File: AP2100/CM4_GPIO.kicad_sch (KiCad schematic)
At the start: 27 parts, among them J1 Conn_01x03, J2 Conn_02x07_Odd_Even, J3 Conn_01x03, J8 THD-20-R, U5 74LVC1G07SE-7, U9 74LVC1G07SE-7

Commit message: Finish PoE section Rename CM4IO library as AP2100
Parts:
- Module1: footprint CM4IO:Raspberry-Pi-4-Compute-Module -> AP2100:Raspberry-Pi-4-Compute-Module; symbol CM4IO:ComputeModule4-CM4 -> AP2100:ComputeModule4-CM4
- U5, U9: symbol CM4IO:74LVC1G07_copy -> AP2100:74LVC1G07_copy
- U? (x4): symbol CM4IO:TPD4EUSB30 -> AP2100:TPD4EUSB30
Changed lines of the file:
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@@
   (junction (at 269.494 63.5) (diameter 1.016) (color 0 0 0 0))
   (junction (at 269.494 68.58) (diameter 1.016) (color 0 0 0 0))
+  (no_connect (at 147.955 109.22))
+  (no_connect (at 147.955 104.14))
+  (no_connect (at 39.37 144.78))
+  (no_connect (at 208.915 111.76))
+  (no_connect (at 208.915 43.18))
   (no_connect (at 147.955 99.06))
   (no_connect (at 147.955 106.68))
-  (no_connect (at 208.915 43.18))
-  (no_connect (at 208.915 111.76))
-  (no_connect (at 147.955 104.14))
-  (no_connect (at 39.37 144.78))
-  (no_connect (at 147.955 109.22))
   (wire (pts (xy 15.24 169.545) (xy 29.21 169.545))
     (stroke (width 0) (type solid) (color 0 0 0 0))
@@
   (symbol (lib_id "power:GND") (at 19.05 57.785 0) (unit 1)
     (in_bom yes) (on_board yes)
-    (property "Reference" "#PWR?" (id 0) (at 19.05 64.135 0)
+    (property "Reference" "#PWR0107" (id 0) (at 19.05 64.135 0)
       (effects (font (size 1.27 1.27)) hide)
     )
@@
   (symbol (lib_id "power:GND") (at 40.64 89.535 0) (unit 1)
     (in_bom yes) (on_board yes)
-    (property "Reference" "#PWR?" (id 0) (at 40.64 95.885 0)
+    (property "Reference" "#PWR0109" (id 0) (at 40.64 95.885 0)
       (effects (font (size 1.27 1.27)) hide)
     )
@@
   (symbol (lib_id "power:GND") (at 66.04 137.795 0) (unit 1)
     (in_bom yes) (on_board yes)
-    (property "Reference" "#PWR?" (id 0) (at 66.04 144.145 0)
+    (property "Reference" "#PWR0111" (id 0) (at 66.04 144.145 0)
       (effects (font (size 1.27 1.27)) hide)
     )
@@
   (symbol (lib_id "power:GND") (at 83.185 57.15 0) (mirror y) (unit 1)
     (in_bom yes) (on_board yes)
-    (property "Reference" "#PWR?" (id 0) (at 83.185 63.5 0)
+    (property "Reference" "#PWR0108" (id 0) (at 83.185 63.5 0)
       (effects (font (size 1.27 1.27)) hide)
     )
@@
   (symbol (lib_id "power:GND") (at 88.9 89.535 0) (unit 1)
     (in_bom yes) (on_board yes)
-    (property "Reference" "#PWR?" (id 0) (at 88.9 95.885 0)
+    (property "Reference" "#PWR0110" (id 0) (at 88.9 95.885 0)
       (effects (font (size 1.27 1.27)) hide)
     )
@@
   (symbol (lib_id "power:GND") (at 93.98 126.365 0) (unit 1)
     (in_bom yes) (on_board yes)
-    (property "Reference" "#PWR?" (id 0) (at 93.98 132.715 0)
+    (property "Reference" "#PWR0114" (id 0) (at 93.98 132.715 0)
       (effects (font (size 1.27 1.27)) hide)
     )
@@
   (symbol (lib_id "power:GND") (at 93.98 158.115 0) (unit 1)
     (in_bom yes) (on_board yes)
-    (property "Reference" "#PWR?" (id 0) (at 93.98 164.465 0)
+    (property "Reference" "#PWR0113" (id 0) (at 93.98 164.465 0)
       (effects (font (size 1.27 1.27)) hide)
     )
@@
     )
   )
-  (symbol (lib_id "CM4IO:74LVC1G07_copy") (at 29.21 177.165 0) (unit 1)
+  (symbol (lib_id "AP2100:74LVC1G07_copy") (at 29.21 177.165 0) (unit 1)
     (in_bom yes) (on_board yes)
     (property "Reference" "U9" (id 0) (at 31.75 170.815 0))
@@
     )
   )
-  (symbol (lib_id "CM4IO:74LVC1G07_copy") (at 152.4 180.34 0) (unit 1)
+  (symbol (lib_id "AP2100:74LVC1G07_copy") (at 152.4 180.34 0) (unit 1)
     (in_bom yes) (on_board yes)
     (property "Reference" "U5" (id 0) (at 153.924 177.8 0)
@@
     )
   )
-  (symbol (lib_id "CM4IO:TPD4EUSB30") (at 40.64 76.835 0) (unit 1)
+  (symbol (lib_id "AP2100:TPD4EUSB30") (at 40.64 76.835 0) (unit 1)
     (in_bom yes) (on_board yes)
     (property "Reference" "U?" (id 0) (at 40.64 64.9732 0))
@@
     )
   )
-  (symbol (lib_id "CM4IO:TPD4EUSB30") (at 88.9 76.835 0) (unit 1)
+  (symbol (lib_id "AP2100:TPD4EUSB30") (at 88.9 76.835 0) (unit 1)
     (in_bom yes) (on_board yes)
     (property "Reference" "U?" (id 0) (at 88.9 64.9732 0))
@@
     )
   )
-  (symbol (lib_id "CM4IO:TPD4EUSB30") (at 93.98 113.665 0) (unit 1)
+  (symbol (lib_id "AP2100:TPD4EUSB30") (at 93.98 113.665 0) (unit 1)
     (in_bom yes) (on_board yes)
     (property "Reference" "U?" (id 0) (at 93.98 101.8032 0))
@@
     )
   )
-  (symbol (lib_id "CM4IO:TPD4EUSB30") (at 93.98 145.415 0) (unit 1)
+  (symbol (lib_id "AP2100:TPD4EUSB30") (at 93.98 145.415 0) (unit 1)
     (in_bom yes) (on_board yes)
     (property "Reference" "U?" (id 0) (at 93.98 133.5532 0))
@@
     )
   )
-  (symbol (lib_id "CM4IO:ComputeModule4-CM4") (at 180.975 76.2 0) (unit 1)
+  (symbol (lib_id "AP2100:ComputeModule4-CM4") (at 180.975 76.2 0) (unit 1)
     (in_bom yes) (on_board yes)
     (property "Reference" "Module1" (id 0) (at 178.435 14.605 0))
     (property "Value" "ComputeModule4" (id 1) (at 178.435 16.9164 0))
-    (property "Footprint" "CM4IO:Raspberry-Pi-4-Compute-Module" (id 2) (at 323.215 102.87 0)
-      (effects (font (size 1.27 1.27)) hide)
-    )
+    (property "Footprint" "AP2100:Raspberry-Pi-4-Compute-Module" (id 2) (at 323.215 102.87 0)
+      (effects (font (size 1.27 1.27)) hide)
+    )

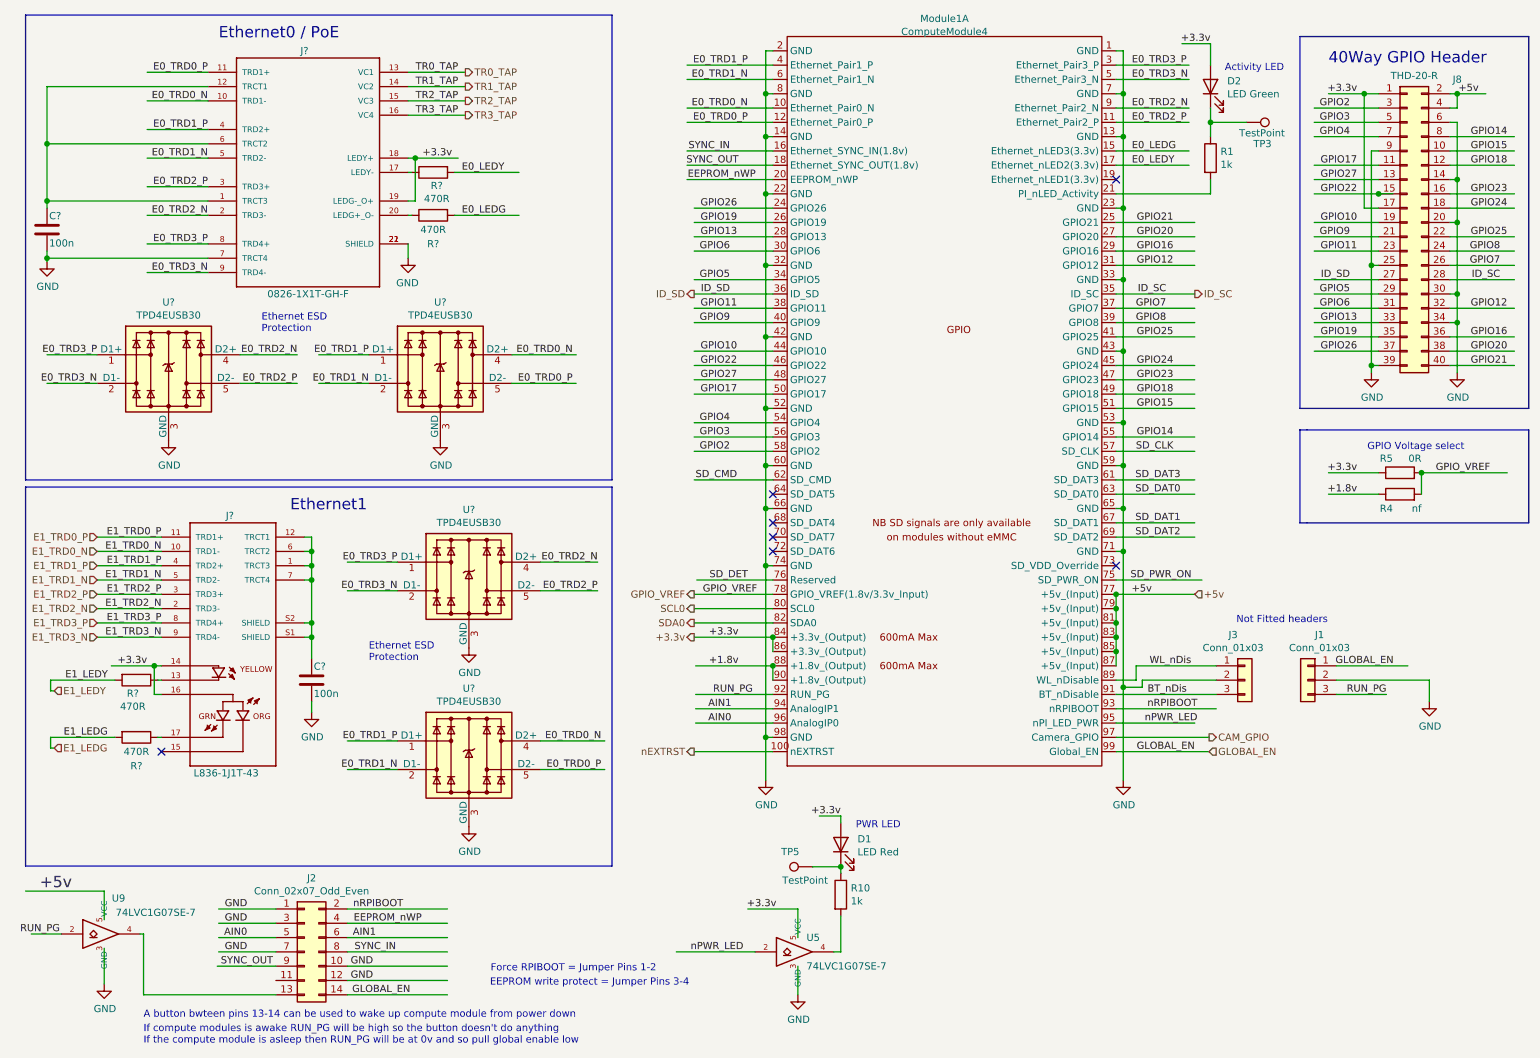
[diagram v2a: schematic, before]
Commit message: Add AP3000 single radio for security cameras. Add CM4IO Raspi board
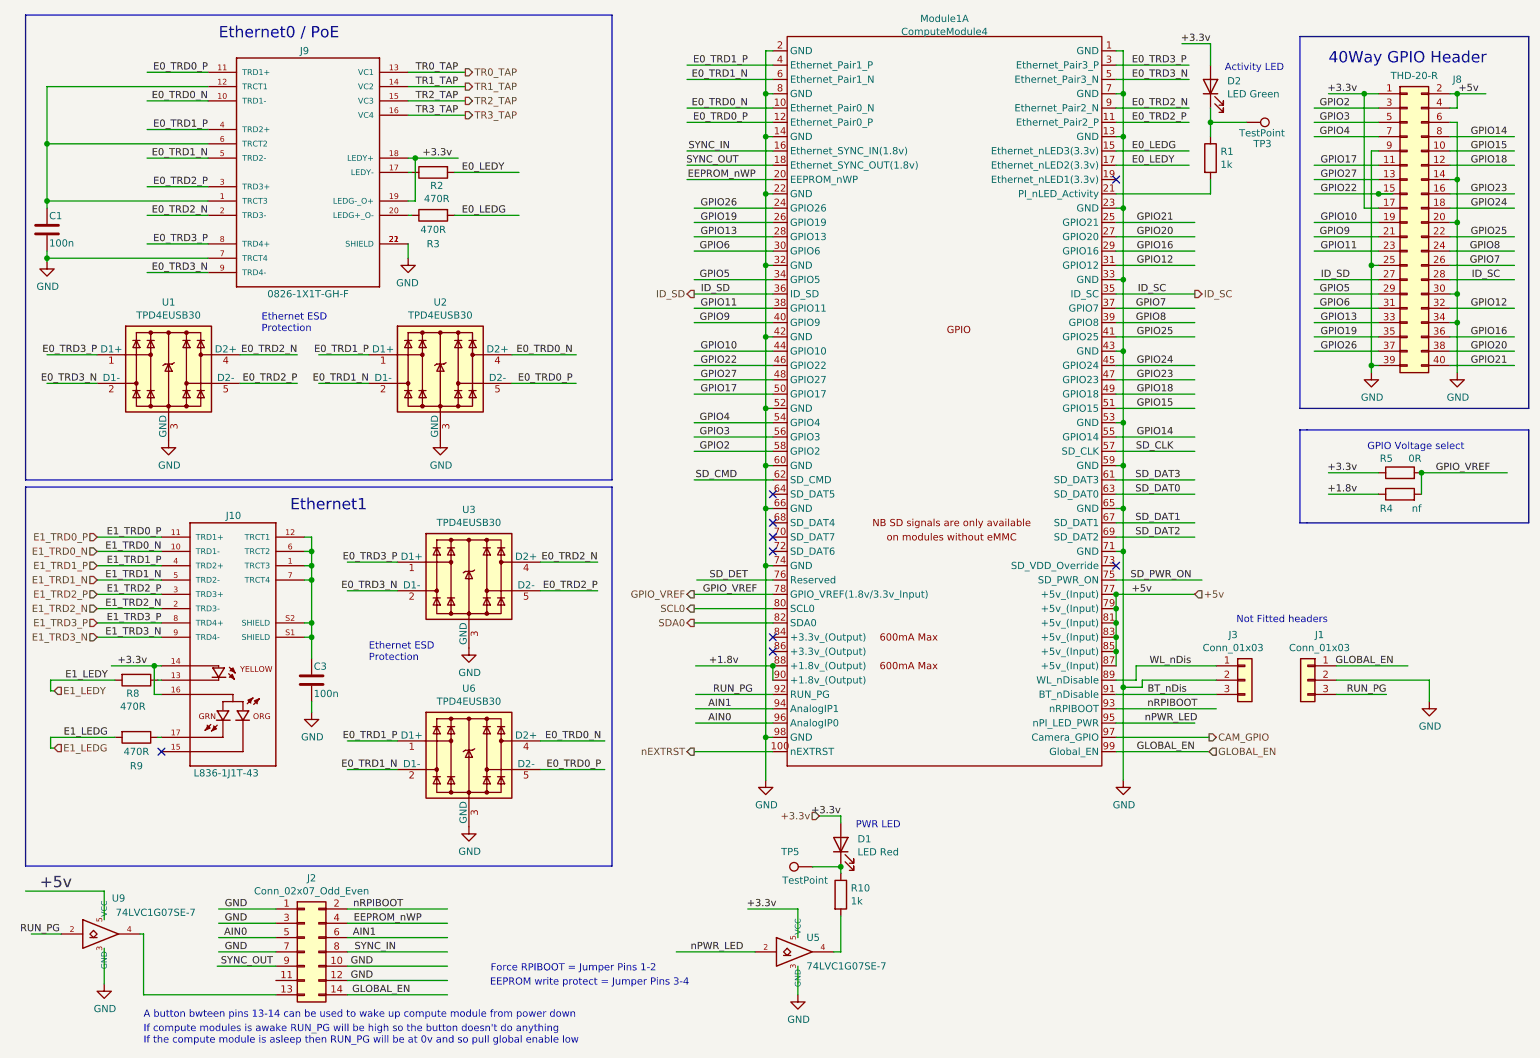
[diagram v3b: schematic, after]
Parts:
- gave numbers to parts that had none: 12
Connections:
- net +3.3v: no longer Module1.84 (+3.3v_(Output)), Module1.86 (+3.3v_(Output))
- no-connect marks 7 -> 9
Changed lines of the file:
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@@
   (junction (at 146.685 111.76) (diameter 1.016) (color 0 0 0 0))
   (junction (at 146.685 142.24) (diameter 1.016) (color 0 0 0 0))
-  (junction (at 147.955 124.46) (diameter 1.016) (color 0 0 0 0))
   (junction (at 147.955 129.54) (diameter 1.016) (color 0 0 0 0))
   (junction (at 160.02 165.227) (diameter 1.016) (color 0 0 0 0))
@@
   (junction (at 269.494 63.5) (diameter 1.016) (color 0 0 0 0))
   (junction (at 269.494 68.58) (diameter 1.016) (color 0 0 0 0))
+  (no_connect (at 208.915 111.76))
+  (no_connect (at 147.955 124.46))
+  (no_connect (at 147.955 127))
   (no_connect (at 208.915 43.18))
   (no_connect (at 147.955 106.68))
+  (no_connect (at 39.37 144.78))
+  (no_connect (at 147.955 99.06))
+  (no_connect (at 147.955 109.22))
   (no_connect (at 147.955 104.14))
-  (no_connect (at 147.955 99.06))
-  (no_connect (at 208.915 111.76))
-  (no_connect (at 147.955 109.22))
-  (no_connect (at 39.37 144.78))
   (wire (pts (xy 15.24 169.545) (xy 29.21 169.545))
     (stroke (width 0) (type solid) (color 0 0 0 0))
@@
     (stroke (width 0) (type solid) (color 0 0 0 0))
   )
-  (wire (pts (xy 133.985 124.46) (xy 147.955 124.46))
-    (stroke (width 0) (type solid) (color 0 0 0 0))
-  )
   (wire (pts (xy 133.985 144.78) (xy 147.955 144.78))
     (stroke (width 0) (type solid) (color 0 0 0 0))
@@
   )
   (wire (pts (xy 147.955 35.56) (xy 146.685 35.56))
-    (stroke (width 0) (type solid) (color 0 0 0 0))
-  )
-  (wire (pts (xy 147.955 127) (xy 147.955 124.46))
     (stroke (width 0) (type solid) (color 0 0 0 0))
   )
@@
     (effects (font (size 1.27 1.27)) (justify right bottom))
   )
-  (label "+3.3v" (at 141.859 124.46 180)
-    (effects (font (size 1.27 1.27)) (justify right bottom))
-  )
   (label "+1.8v" (at 141.859 129.54 180)
     (effects (font (size 1.27 1.27)) (justify right bottom))
@@
     (effects (font (size 1.27 1.27)) (justify right))
   )
-  (hierarchical_label "+3.3v" (shape output) (at 133.985 124.46 180)
-    (effects (font (size 1.27 1.27)) (justify right))
-  )
   (hierarchical_label "nEXTRST" (shape output) (at 133.985 144.78 180)
     (effects (font (size 1.27 1.27)) (justify right))
   )
+  (hierarchical_label "+3.3v" (shape input) (at 156.21 156.21 180)
+    (effects (font (size 1.27 1.27)) (justify right))
+  )
   (hierarchical_label "ID_SC" (shape output) (at 222.885 63.5 0)
     (effects (font (size 1.27 1.27)) (justify left))
@@
   (symbol (lib_id "Device:R") (at 34.925 132.08 270) (unit 1)
     (in_bom yes) (on_board yes)
-    (property "Reference" "R?" (id 0) (at 34.29 134.4422 90))
+    (property "Reference" "R8" (id 0) (at 34.29 134.4422 90))
     (property "Value" "470R" (id 1) (at 34.29 136.7536 90))
     (property "Footprint" "Resistor_SMD:R_0402_1005Metric" (id 2) (at 34.925 130.302 90)
@@
   (symbol (lib_id "Device:R") (at 34.925 142.24 270) (unit 1)
     (in_bom yes) (on_board yes)
-    (property "Reference" "R?" (id 0) (at 34.925 147.32 90))
+    (property "Reference" "R9" (id 0) (at 34.925 147.32 90))
     (property "Value" "470R" (id 1) (at 34.925 144.78 90))
     (property "Footprint" "Resistor_SMD:R_0402_1005Metric" (id 2) (at 34.925 140.462 90)
@@
   (symbol (lib_id "Device:R") (at 87.63 41.91 90) (mirror x) (unit 1)
     (in_bom yes) (on_board yes)
-    (property "Reference" "R?" (id 0) (at 88.265 44.2722 90))
+    (property "Reference" "R2" (id 0) (at 88.265 44.2722 90))
     (property "Value" "470R" (id 1) (at 88.265 46.5836 90))
     (property "Footprint" "Resistor_SMD:R_0402_1005Metric" (id 2) (at 87.63 40.132 90)
@@
   (symbol (lib_id "Device:R") (at 87.63 49.53 90) (mirror x) (unit 1)
     (in_bom yes) (on_board yes)
-    (property "Reference" "R?" (id 0) (at 87.63 54.61 90))
+    (property "Reference" "R3" (id 0) (at 87.63 54.61 90))
     (property "Value" "470R" (id 1) (at 87.63 52.07 90))
     (property "Footprint" "Resistor_SMD:R_0402_1005Metric" (id 2) (at 87.63 47.752 90)
@@
   (symbol (lib_id "Device:C") (at 19.05 52.07 0) (unit 1)
     (in_bom yes) (on_board yes)
-    (property "Reference" "C?" (id 0) (at 19.431 49.6316 0)
+    (property "Reference" "C1" (id 0) (at 19.431 49.6316 0)
       (effects (font (size 1.27 1.27)) (justify left))
     )
@@
   (symbol (lib_id "Device:C") (at 66.04 132.08 0) (unit 1)
     (in_bom yes) (on_board yes)
-    (property "Reference" "C?" (id 0) (at 66.421 129.6416 0)
+    (property "Reference" "C3" (id 0) (at 66.421 129.6416 0)
       (effects (font (size 1.27 1.27)) (justify left))
     )
@@
   (symbol (lib_id "AP2100:TPD4EUSB30") (at 40.64 76.835 0) (unit 1)
     (in_bom yes) (on_board yes)
-    (property "Reference" "U?" (id 0) (at 40.64 64.9732 0))
+    (property "Reference" "U1" (id 0) (at 40.64 64.9732 0))
     (property "Value" "TPD4EUSB30" (id 1) (at 40.64 67.2846 0))
     (property "Footprint" "Package_SON:USON-10_2.5x1.0mm_P0.5mm" (id 2) (at 16.51 86.995 0)
@@
   (symbol (lib_id "AP2100:TPD4EUSB30") (at 88.9 76.835 0) (unit 1)
     (in_bom yes) (on_board yes)
-    (property "Reference" "U?" (id 0) (at 88.9 64.9732 0))
+    (property "Reference" "U2" (id 0) (at 88.9 64.9732 0))
     (property "Value" "TPD4EUSB30" (id 1) (at 88.9 67.2846 0))
     (property "Footprint" "Package_SON:USON-10_2.5x1.0mm_P0.5mm" (id 2) (at 64.77 86.995 0)
@@
   (symbol (lib_id "AP2100:TPD4EUSB30") (at 93.98 113.665 0) (unit 1)
     (in_bom yes) (on_board yes)
-    (property "Reference" "U?" (id 0) (at 93.98 101.8032 0))
+    (property "Reference" "U3" (id 0) (at 93.98 101.8032 0))
     (property "Value" "TPD4EUSB30" (id 1) (at 93.98 104.1146 0))
     (property "Footprint" "Package_SON:USON-10_2.5x1.0mm_P0.5mm" (id 2) (at 69.85 123.825 0)
@@
   (symbol (lib_id "AP2100:TPD4EUSB30") (at 93.98 145.415 0) (unit 1)
     (in_bom yes) (on_board yes)
-    (property "Reference" "U?" (id 0) (at 93.98 133.5532 0))
+    (property "Reference" "U6" (id 0) (at 93.98 133.5532 0))
     (property "Value" "TPD4EUSB30" (id 1) (at 93.98 135.8646 0))
     (property "Footprint" "Package_SON:USON-10_2.5x1.0mm_P0.5mm" (id 2) (at 69.85 155.575 0)
@@
   (symbol (lib_id "L836-1J1T-43:L836-1J1T-43") (at 52.07 127 0) (unit 1)
     (in_bom yes) (on_board yes)
-    (property "Reference" "J?" (id 0) (at 50.8 102.87 0)
+    (property "Reference" "J10" (id 0) (at 50.8 102.87 0)
       (effects (font (size 1.27 1.27)) (justify left))
     )
@@
   (symbol (lib_id "0826-1X1T-GH-F:0826-1X1T-GH-F") (at 65.405 41.91 0) (unit 1)
     (in_bom yes) (on_board yes)
-    (property "Reference" "J?" (id 0) (at 64.77 20.32 0))
+    (property "Reference" "J9" (id 0) (at 64.77 20.32 0))
     (property "Value" "0826-1X1T-GH-F" (id 1) (at 65.405 63.5 0))
     (property "Footprint" "BEL_0826-1X1T-GH-F" (id 2) (at 65.405 41.91 0)
